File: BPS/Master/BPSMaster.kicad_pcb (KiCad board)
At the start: 2 copper layers, 100 x 75 mm, 180 parts, among them J1 SWD, J10 DisplayJumper, J11 FrontFans, J12 BackFans, J13 ErrorLightConnector, J14 Conn_01x03, J2 Logic Analyzer, J3 CurrentSlaveConnector, J4 CarPowerConnector, J5 CAN_Out, J6 ContactorConnector, J7 VoltageSlaveConnector, J8 DisplayConnector, J9 TempSlaveConnector, Q1 VND5N07-E, Q2 NVR4003NT3G, Q3 NVR4003NT3G, Q4 NVR4003NT3G, SW1 B3SL-1002P, U1 STM32F413RHTx, U10 LTC6820, U11 HX1188FNL, U12 LTC6820, U13 Si8641EC-B-IS1, U14 SI8660EC-B-IS1, U15 RI3-1205S, U16 SI8261ABC-IS, U2 RI3-1205S, U3 NCP1117-3.3_SOT223, U4 CDSOT23-T24CAN, U5 ADM3055E, U6 BAS70-04, U7 SI8261ABC-IS, U8 M24128, Y1 NX8045GB-8.000M-STD-CSJ-1

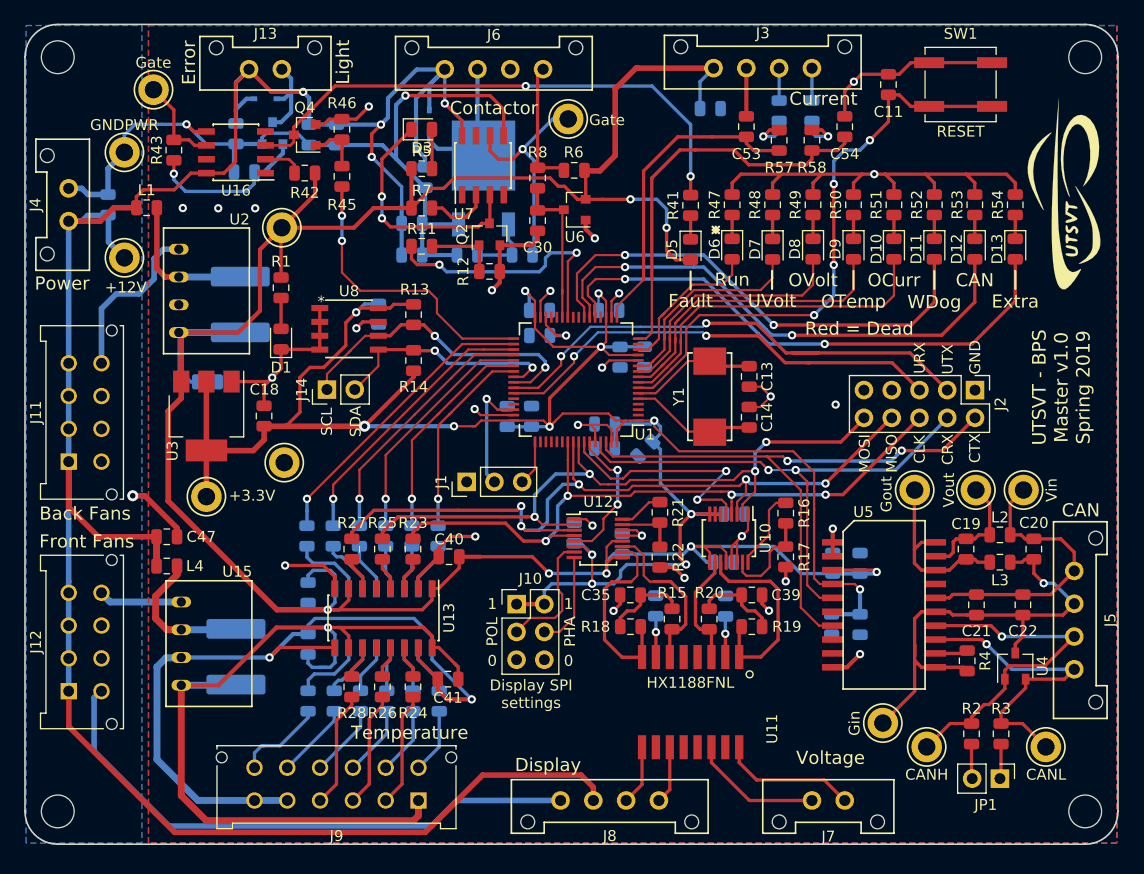
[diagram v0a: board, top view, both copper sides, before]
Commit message: Edited inductor choke in BPS master.
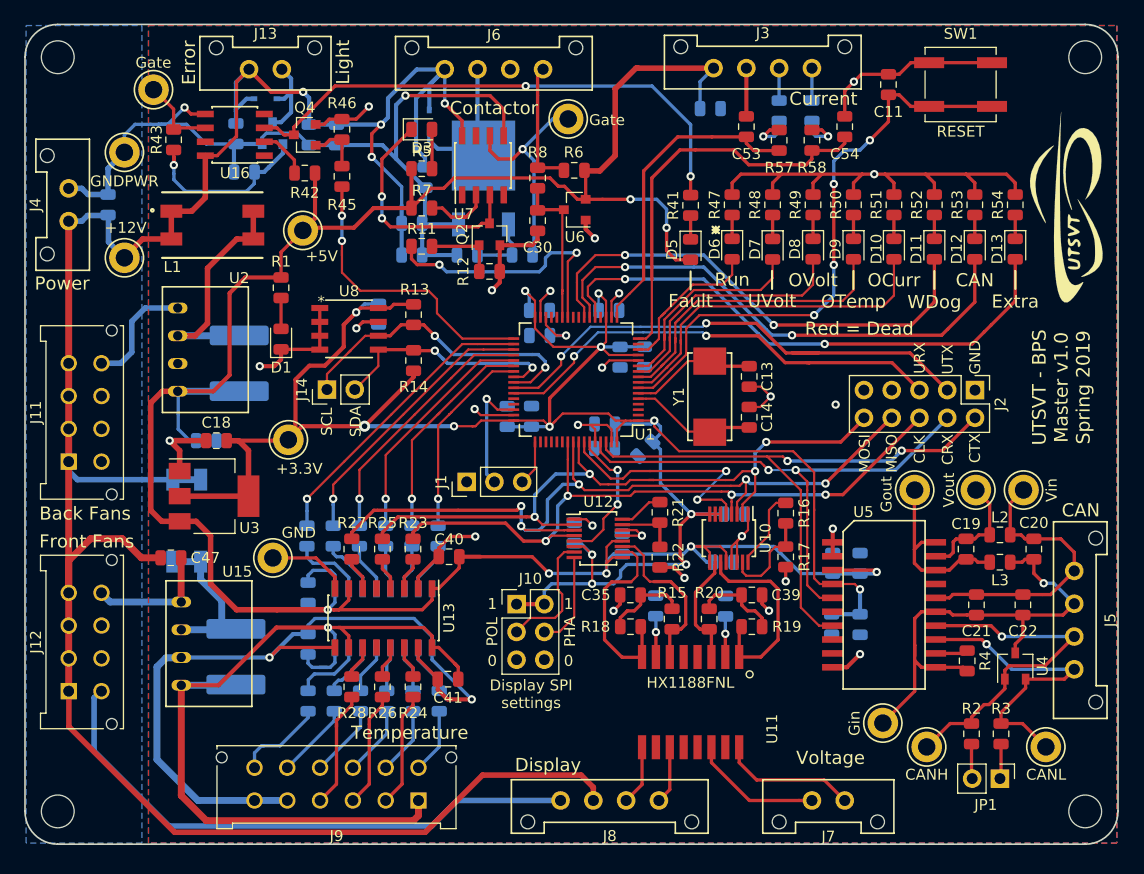
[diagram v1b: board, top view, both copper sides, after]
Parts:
- L1: footprint Inductor_SMD:L_0805_2012Metric -> UTSVT_BPS:SRF0905A
- L4: footprint Inductor_SMD:L_0805_2012Metric -> UTSVT_BPS:SRF0905A; moved to B.Cu
- moved TP4 9.13 mm to (124.1, 113.0)
- moved TP3 8.78 mm to (122.7, 123.8)
- moved U3 7.37 mm to (117.3, 118.2), turned to 0 degrees
- moved L1 6.22 mm to (117.1, 93.4)
- moved C15 5.38 mm to (119.6, 106.0)
- moved C17 5.38 mm to (116.6, 113.1)
- moved U2 5.38 mm to (114.0, 104.8)
- moved C18 4.91 mm to (117.5, 113.1), turned to 180 degrees
- moved L4 4.53 mm to (114.8, 120.4), turned to 270 degrees
- moved C47 1.96 mm to (113.3, 123.8)
- moved TP2 1.94 mm to (125.4, 93.8)
- moved U16 1.60 mm to (119.2, 85.1)
- moved G*** 1.22 mm to (195.4, 92.0)
- moved R43 0.95 mm to (113.6, 85.5)
- moved G*** 0.40 mm to (165.6, 94.2)
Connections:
- L1 pad 2: Net-(C15-Pad1) -> +12V
- L4 pad 2: Net-(C46-Pad1) -> +12V
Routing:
- net +12V: track 221.8 -> 230.3 mm
- net Net-(C15-Pad1): track 13.5 -> 21.7 mm
- net GNDPWR: track 158.2 -> 154.7 mm, vias 3 -> 2
- net Net-(C46-Pad1): track 13.4 -> 14.9 mm
- net GND: track 162.9 -> 164.3 mm, vias 25 -> 24
- net Net-(Q3-Pad1): track 15.1 -> 16.4 mm
- net Net-(R43-Pad2): track 8.55 -> 7.38 mm
- net Net-(R42-Pad1): track 3.60 -> 4.64 mm
- net +3V3: track 215.0 -> 215.5 mm
- net (no net): vias 3 -> 1

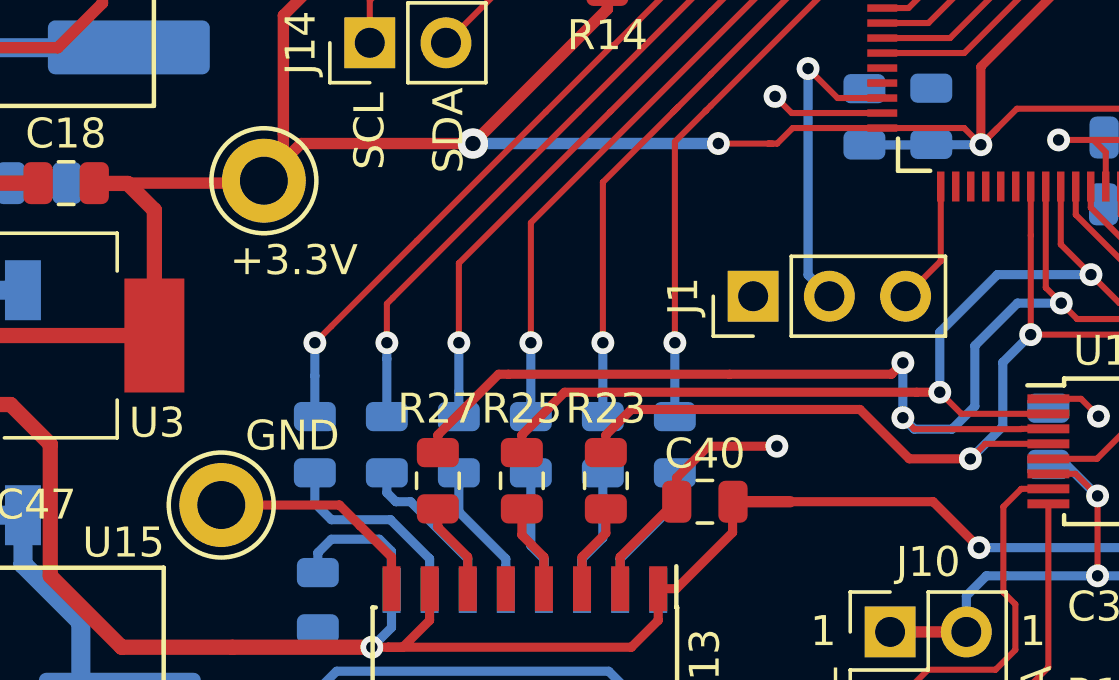
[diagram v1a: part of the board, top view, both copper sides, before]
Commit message: Added labels to USB breakout.
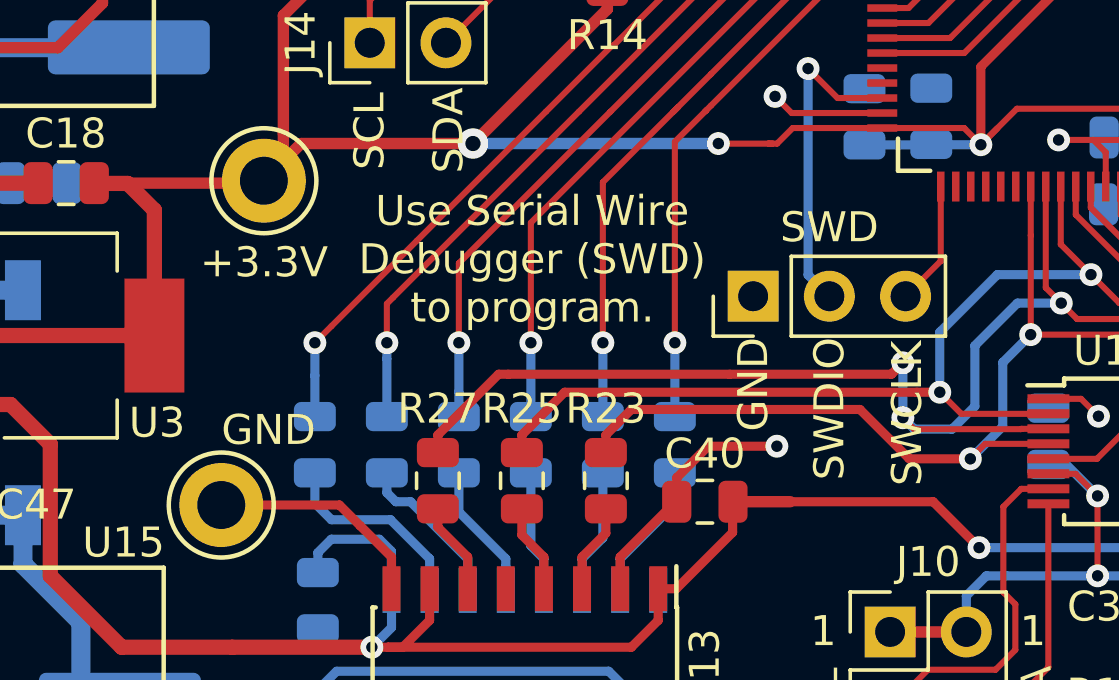
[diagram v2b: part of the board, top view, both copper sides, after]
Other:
- board text added: "SWCLK"
- board text added: "SWD"
- board text added: "SWDIO"
- board text added: "Use Serial Wire Debugger (SWD) to program."
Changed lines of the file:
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@@
   (general
     (thickness 1.6)
-    (drawings 123)
+    (drawings 128)
     (tracks 1505)
     (zones 0)
@@
     (descr "Through hole straight pin header, 1x03, 2.54mm pitch, single row")
     (tags "Through hole pin header THT 1x03 2.54mm single row")
-    (fp_text reference J1 (at 0 -2.33 90) (layer F.SilkS)
+    (fp_text reference J1 (at 2.296 2.5412 180) (layer F.SilkS) hide
       (effects (font (size 1 1) (thickness 0.15)))
     )
@@
     )
   )
+  (gr_text SWD (at 142.9512 114.554) (layer F.SilkS)
+    (effects (font (size 1 1) (thickness 0.15)))
+  )
+  (gr_text "Use Serial Wire\nDebugger (SWD)\nto program." (at 133.0452 115.6208) (layer F.SilkS)
+    (effects (font (size 1 1) (thickness 0.15)))
+  )
+  (gr_text SWCLK (at 145.542 120.7516 90) (layer F.SilkS)
+    (effects (font (size 1 1) (thickness 0.15)))
+  )
+  (gr_text SWDIO (at 142.9512 120.5992 90) (layer F.SilkS)
+    (effects (font (size 1 1) (thickness 0.15)))
+  )
+  (gr_text GND (at 140.4112 119.7864 90) (layer F.SilkS)
+    (effects (font (size 1 1) (thickness 0.15)))
+  )
   (gr_text +5V (at 127.15 96.2) (layer F.SilkS)
     (effects (font (size 1 1) (thickness 0.15)))
   )
-  (gr_text GND (at 125.05 121.5) (layer F.SilkS)
+  (gr_text GND (at 124.2568 121.3104) (layer F.SilkS)
     (effects (font (size 1 1) (thickness 0.15)))
   )
@@
   (gr_line (start 103 75) (end 197 75) (layer Edge.Cuts) (width 0.15))
   (gr_line (start 100 147) (end 100 78) (layer Edge.Cuts) (width 0.15))
-  (gr_text +3.3V (at 125.1 115.65) (layer F.SilkS)
+  (gr_text +3.3V (at 124.1044 115.7224) (layer F.SilkS)
     (effects (font (size 1 1) (thickness 0.15)))
   )

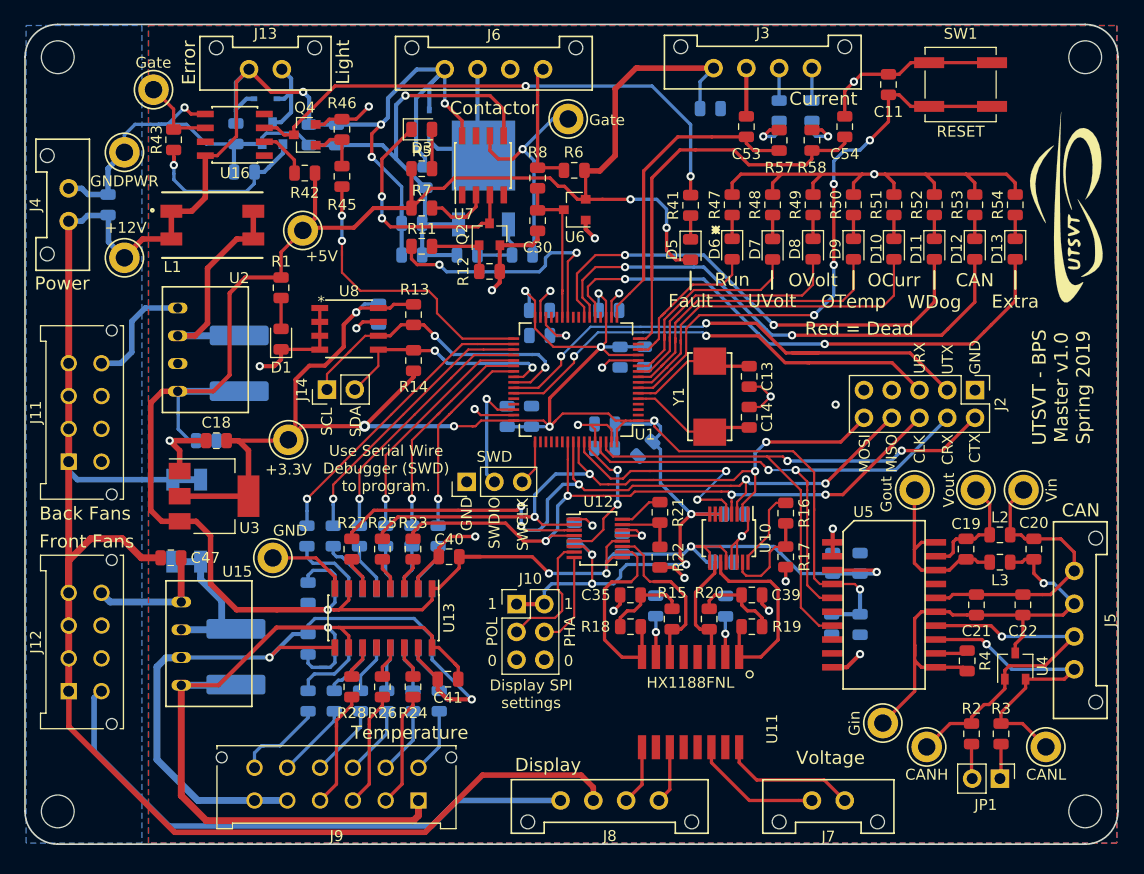
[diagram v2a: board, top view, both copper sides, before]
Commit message: Updated BPS pcbs.
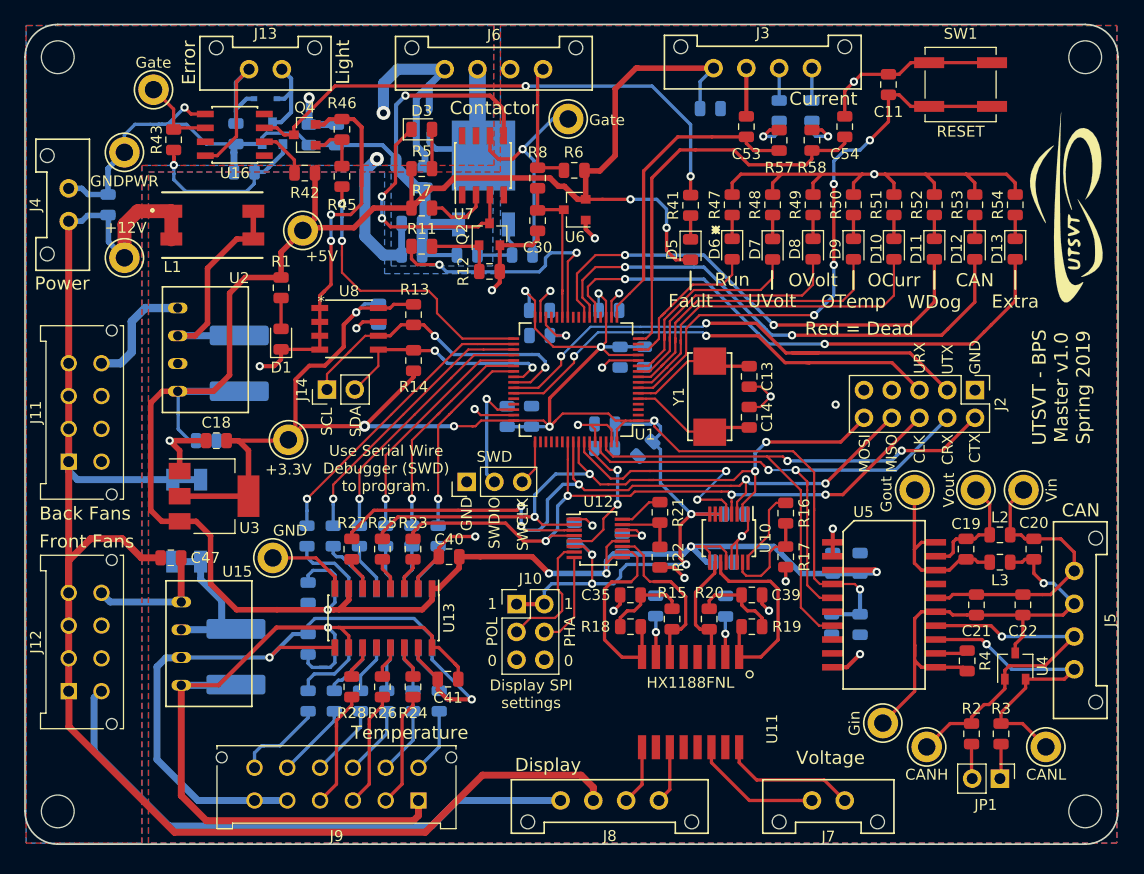
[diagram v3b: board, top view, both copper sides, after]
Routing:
- net +12V: track 230.3 -> 207.4 mm, vias 4 -> 3
- net GND: track 164.3 -> 183.2 mm, vias 24 -> 25
- added copper zone on F.Cu, net +12V
